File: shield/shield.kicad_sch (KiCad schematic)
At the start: 42 parts, among them J1 Screw_Terminal_01x02, J2 Screw_Terminal_01x02, J3 IC Side 1, J4 IC Side 2, J5 Power Side 1, J6 Power Side 2, Q1 GAN3R2-100CBE, Q2 GAN3R2-100CBE, U1 LM74900

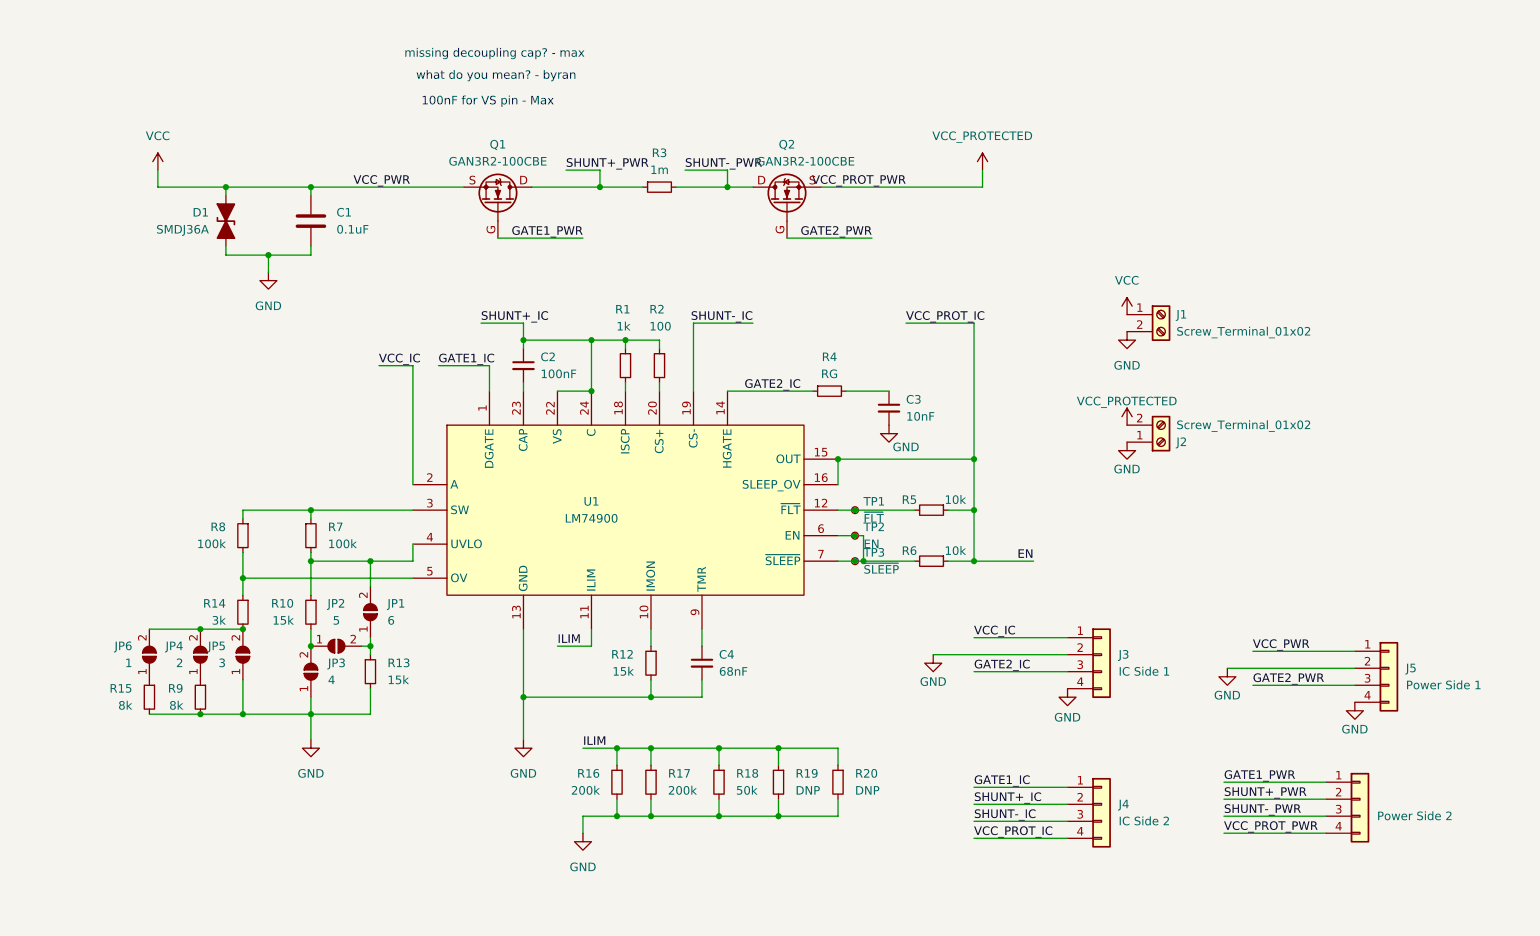
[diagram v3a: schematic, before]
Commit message: Fix: revised shield schematic and pcb
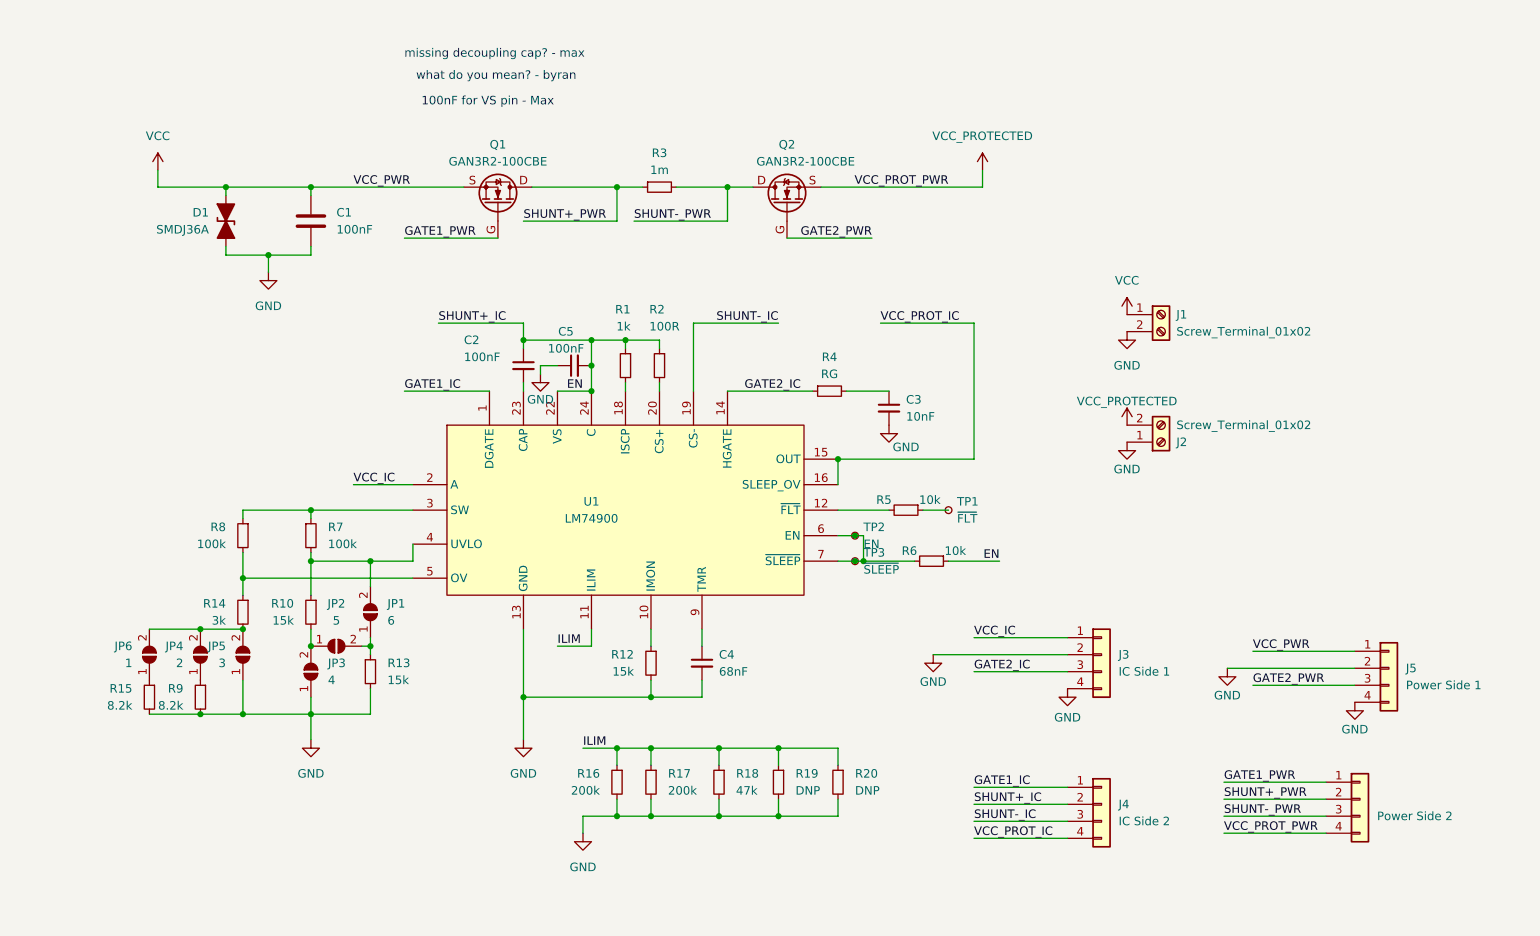
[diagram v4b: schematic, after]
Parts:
- added C5: 100nF, Capacitor_SMD:C_0603_1608Metric, symbol Device:C_Small
- C1: value 0.1uF -> 100nF
- R15, R9: value 8k -> 8.2k
- R18: value 50k -> 47k
- R2: value 100 -> 100R
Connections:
- net SHUNT+_IC is gone; now on net EN: C2.1, J4.2 (Pin_2), R1.1, R2.1, U1.22 (VS), U1.24 (C)
- net EN: now also C5.2; no longer J4.4 (Pin_4), R5.1, U1.15 (OUT), U1.16 (SLEEP_OV)
- net GND: now also C5.1
- net at R5.2, U1.12 (~{FLT}): no longer TP1.1
- new net: R5.1, TP1.1
- new net VCC_PROT_IC: J4.4 (Pin_4), U1.15 (OUT), U1.16 (SLEEP_OV)
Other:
- moved on the sheet: R5, TP1

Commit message: Feat(shield): finished pcb
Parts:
- added Q3, Q4: EPC2304, EPC2304ENGRT:EPC2304_ECC, symbol NFET:Q_NMOS_GSD
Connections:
- net GATE1_PWR: now also Q3.G
- net GATE2_PWR: now also Q4.G
- net SHUNT+_PWR: now also Q3.D
- net SHUNT-_PWR: now also Q4.D
- net VCC: now also Q3.S
- net VCC_PROTECTED: now also Q4.S
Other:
- note removed: "100nF for VS pin - Max"
- note removed: "missing decoupling cap? - max"
- note removed: "what do you mean? - byran"
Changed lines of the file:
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@@
+	(wire
+		(pts
+			(xy 156.21 46.482) (xy 175.26 46.482)
+		)
+		(stroke
+			(width 0)
+			(type default)
+		)
+	)
 	(wire
 		(pts
@@
 	(wire
 		(pts
+			(xy 107.95 54.356) (xy 93.98 54.356)
+		)
+		(stroke
+			(width 0)
+			(type default)
+		)
+	)
+	(wire
+		(pts
 			(xy 93.98 95.25) (xy 106.68 95.25)
 		)
@@
 	(wire
 		(pts
+			(xy 151.13 54.102) (xy 163.83 54.102)
+		)
+		(stroke
+			(width 0)
+			(type default)
+		)
+	)
+	(wire
+		(pts
 			(xy 142.24 95.25) (xy 154.94 95.25)
 		)
@@
 	(wire
 		(pts
+			(xy 132.08 46.482) (xy 146.05 46.482)
+		)
+		(stroke
+			(width 0)
+			(type default)
+		)
+	)
+	(wire
+		(pts
+			(xy 93.218 46.736) (xy 102.87 46.736)
+		)
+		(stroke
+			(width 0)
+			(type default)
+		)
+	)
+	(wire
+		(pts
 			(xy 116.84 91.44) (xy 114.3 91.44)
 		)
@@
 	(wire
 		(pts
+			(xy 127 46.736) (xy 113.03 46.736)
+		)
+		(stroke
+			(width 0)
+			(type default)
+		)
+	)
+	(wire
+		(pts
 			(xy 220.726 134.112) (xy 235.966 134.112)
 		)
@@
 			(width 0)
 			(type default)
-		)
-	)
-	(text "100nF for VS pin - Max"
-		(exclude_from_sim no)
-		(at 106.426 52.07 0)
-		(effects
-			(font
-				(size 1.27 1.27)
-			)
-		)
-	)
-	(text "what do you mean? - byran"
-		(exclude_from_sim no)
-		(at 107.696 48.26 0)
-		(effects
-			(font
-				(size 1.27 1.27)
-			)
-		)
-	)
-	(text "missing decoupling cap? - max"
-		(exclude_from_sim no)
-		(at 107.442 44.958 0)
-		(effects
-			(font
-				(size 1.27 1.27)
-			)
 		)
 	)
@@
 		)
 	)
+	(label "GATE2_PWR"
+		(at 163.83 54.102 180)
+		(fields_autoplaced yes)
+		(effects
+			(font
+				(size 1.27 1.27)
+			)
+			(justify right bottom)
+		)
+	)
+	(label "SHUNT+_PWR"
+		(at 127 46.736 180)
+		(fields_autoplaced yes)
+		(effects
+			(font
+				(size 1.27 1.27)
+			)
+			(justify right bottom)
+		)
+	)
+	(label "SHUNT-_PWR"
+		(at 132.08 46.482 0)
+		(fields_autoplaced yes)
+		(effects
+			(font
+				(size 1.27 1.27)
+			)
+			(justify left bottom)
+		)
+	)
 	(label "EN"
 		(at 182.88 120.65 180)
@@
 		)
 	)
+	(label "GATE1_PWR"
+		(at 93.98 54.356 0)
+		(fields_autoplaced yes)
+		(effects
+			(font
+				(size 1.27 1.27)
+			)
+			(justify left bottom)
+		)
+	)
 	(label "ILIM"
 		(at 120.65 148.59 0)
@@
 		)
 	)
+	(label "VCC_PROT_PWR"
+		(at 175.26 46.482 180)
+		(fields_autoplaced yes)
+		(effects
+			(font
+				(size 1.27 1.27)
+			)
+			(justify right bottom)
+		)
+	)
 	(label "GATE2_PWR"
 		(at 163.83 72.39 180)
@@
 			)
 			(justify right bottom)
+		)
+	)
+	(label "VCC_PWR"
+		(at 93.218 46.736 0)
+		(fields_autoplaced yes)
+		(effects
+			(font
+				(size 1.27 1.27)
+			)
+			(justify left bottom)
 		)
 	)
@@
 	)
 	(symbol
+		(lib_id "NFET:Q_NMOS_GSD")
+		(at 151.13 49.022 90)
+		(unit 1)
+		(exclude_from_sim no)
+		(in_bom yes)
+		(on_board yes)
+		(dnp no)
+		(property "Reference" "Q4"
+			(at 151.13 40.132 90)
+			(effects
+				(font
+					(size 1.27 1.27)
+				)
+			)
+		)
+		(property "Value" "EPC2304"
+			(at 153.924 42.672 90)
+			(effects
+				(font
+					(size 1.27 1.27)
+				)
+				(justify left)
+			)
+		)
+		(property "Footprint" "EPC2304ENGRT:EPC2304_ECC"
+			(at 148.59 43.942 0)
+			(effects
+				(font
+					(size 1.27 1.27)
+				)
+				(hide yes)
+			)
+		)
+		(property "Datasheet" "~"
+			(at 151.13 49.022 0)
+			(effects
+				(font
+					(size 1.27 1.27)
+				)
+				(hide yes)
+			)
+		)
+		(property "Description" "N-MOSFET transistor, gate/source/drain"
+			(at 151.13 49.022 0)
+			(effects
+				(font
+					(size 1.27 1.27)
+				)
+				(hide yes)
+			)
+		)
+		(pin "G"
+		)
+		(pin "D"
+		)
+		(pin "S"
+		)
+		(instances
+			(project "shield"
+				(path "/5b82dc35-3a33-40e8-9adc-c72e6c4a87f2"
+					(reference "Q4")
+					(unit 1)
+				)
+			)
+		)
+	)
+	(symbol
 		(lib_id "Connector_Generic:Conn_01x04")
 		(at 198.12 156.972 0)
@@
 					(unit 1)
 				)
+			)
+		)
+	)
+	(symbol
+		(lib_id "NFET:Q_NMOS_GSD")
+		(at 107.95 49.276 270)
+		(mirror x)
+		(unit 1)
+		(exclude_from_sim no)
+		(in_bom yes)
+		(on_board yes)
+		(dnp no)
+		(property "Reference" "Q3"
+			(at 107.95 40.386 90)
+			(effects
+				(font
+					(size 1.27 1.27)
+				)
+			)
+		)
+		(property "Value" "EPC2304"
+			(at 107.95 42.926 90)
+			(effects
+				(font
+					(size 1.27 1.27)
+				)
+			)
+		)
+		(property "Footprint" "EPC2304ENGRT:EPC2304_ECC"
+			(at 110.49 44.196 0)
+			(effects
+				(font
+					(size 1.27 1.27)
+				)
+				(hide yes)
+			)
+		)
+		(property "Datasheet" "~"
+			(at 107.95 49.276 0)
+			(effects
+				(font
+					(size 1.27 1.27)
+				)
+				(hide yes)
+			)
+		)
+		(property "Description" "N-MOSFET transistor, gate/source/drain"
+			(at 107.95 49.276 0)
+			(effects
+				(font
+					(size 1.27 1.27)
+				)
+				(hide yes)
+			)
+		)
+		(pin "G"
+		)
+		(pin "D"
+		)
+		(pin "S"
+		)
+		(instances
+			(project "shield"
+				(path "/5b82dc35-3a33-40e8-9adc-c72e6c4a87f2"
+					(reference "Q3")
+					(unit 1)
+				)

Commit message: Fix: panelized shield
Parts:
- R14: value 3k -> 4.22k
- R15, R9: value 8.2k -> 15k
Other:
- note added: "OVLO 14.82V: JP #3 OVLO 5.72V: JP #1, JP #2 OVLO 3.72V: JP #2"
- note added: "Selectable OVLO/UVLO, bridge jumpers:"
- note added: "UVLO 8.6V: JP #4, JP #6 UVLO 4.6V: JP #4 UVLO 2.6V: JP #5"
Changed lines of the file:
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@@
 		)
 	)
+	(text "UVLO 8.6V: JP #4, JP #6\nUVLO 4.6V: JP #4\nUVLO 2.6V: JP #5"
+		(exclude_from_sim no)
+		(at 52.07 165.1 0)
+		(effects
+			(font
+				(size 1.27 1.27)
+			)
+			(justify left)
+		)
+	)
+	(text "OVLO 14.82V: JP #3\nOVLO 5.72V: JP #1, JP #2\nOVLO 3.72V: JP #2"
+		(exclude_from_sim no)
+		(at 52.07 171.45 0)
+		(effects
+			(font
+				(size 1.27 1.27)
+			)
+			(justify left)
+		)
+	)
+	(text "Selectable OVLO/UVLO, bridge jumpers:"
+		(exclude_from_sim no)
+		(at 68.58 160.02 0)
+		(effects
+			(font
+				(size 1.27 1.27)
+				(thickness 0.254)
+				(bold yes)
+				(italic yes)
+			)
+		)
+	)
 	(label "SHUNT-_IC"
 		(at 179.07 159.512 0)
@@
 			)
 		)
-		(property "Value" "8.2k"
+		(property "Value" "15k"
 			(at 60.96 142.2399 0)
 			(effects
@@
 			)
 		)
-		(property "Value" "8.2k"
+		(property "Value" "15k"
 			(at 53.34 142.2399 0)
 			(effects
@@
 			)
 		)
-		(property "Value" "3k"
+		(property "Value" "4.22k"
 			(at 67.31 129.5399 0)
 			(effects

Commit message: Feat[shield]: schematic draft
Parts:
- removed C2, C5: 100nF, Capacitor_SMD:C_0603_1608Metric, symbol Device:C_Small
- removed C3: 10nF, Capacitor_SMD:C_0603_1608Metric, symbol Device:C_Small
- removed C4: 68nF, Capacitor_SMD:C_0603_1608Metric, symbol Device:C_Small
- removed JP4: 2, Jumper:SolderJumper-2_P1.3mm_Open_Pad1.0x1.5mm, symbol Jumper:SolderJumper_2_Open
- removed JP5: 3, Jumper:SolderJumper-2_P1.3mm_Open_Pad1.0x1.5mm, symbol Jumper:SolderJumper_2_Open
- removed JP6: 1, Jumper:SolderJumper-2_P1.3mm_Open_Pad1.0x1.5mm, symbol Jumper:SolderJumper_2_Open
- removed R10, R12, R13, R15: 15k, Resistor_SMD:R_0402_1005Metric, symbol Device:R_Small
- removed R14: 4.22k, Resistor_SMD:R_0402_1005Metric, symbol Device:R_Small
- removed R16, R17: 200k, Resistor_SMD:R_0402_1005Metric, symbol Device:R_Small
- removed R18: 47k, Resistor_SMD:R_0402_1005Metric, symbol Device:R_Small
- removed R19, R20: DNP, Resistor_SMD:R_0603_1608Metric, symbol Device:R_Small
- removed TP1: ~{FLT}, TestPoint:TestPoint_Pad_1.0x1.0mm, symbol Connector:TestPoint_Small
- removed TP2: EN, TestPoint:TestPoint_Pad_1.0x1.0mm, symbol Connector:TestPoint_Small
- removed TP3: ~{SLEEP}, TestPoint:TestPoint_Pad_1.0x1.0mm, symbol Connector:TestPoint_Small
- removed U1: LM74900, Package_DFN_QFN:VQFN-24-1EP_4x4mm_P0.5mm_EP2.5x2.5mm, symbol LM74900:LM74900
- added C2, C4: 100nF, Capacitor_SMD:C_1206_3216Metric, symbol Device:C
- added C3: 10nF, Capacitor_SMD:C_1206_3216Metric, symbol Device:C
- added C5: 47uF, Capacitor_SMD:C_1206_3216Metric, symbol Device:C
- added U1: LM74810QDRRRQ1, SON50P300X300X80-13N-D, symbol LM74810QDRRRQ1:LM74810QDRRRQ1
- JP1: value 6 -> SolderJumper_2_Open; footprint Jumper:SolderJumper-2_P1.3mm_Open_Pad1.0x1.5mm -> (none)
- JP2: value 5 -> SolderJumper_2_Open; footprint Jumper:SolderJumper-2_P1.3mm_Open_Pad1.0x1.5mm -> (none)
- JP3: value 4 -> SolderJumper_2_Open; footprint Jumper:SolderJumper-2_P1.3mm_Open_Pad1.0x1.5mm -> (none)
- Q1, Q2: value GAN3R2-100CBE -> IRFB3077PbF
- Q3, Q4: value EPC2304 -> IPB020N10N5LF; footprint EPC2304ENGRT:EPC2304_ECC -> WLCSP8-SOT8072:WLCSP8-SOT8072
- R1: value 1k -> 22kΩ; footprint Resistor_SMD:R_0402_1005Metric -> (none)
- R2: value 100R -> 22kΩ; footprint Resistor_SMD:R_0402_1005Metric -> (none)
- R3: value 1m -> 3.3kΩ; footprint Resistor_SMD:R_2512_6332Metric -> (none)
- R4: value RG -> 100kΩ; footprint Resistor_SMD:R_0402_1005Metric -> (none)
- R5: value 10k -> 220kΩ; footprint Resistor_SMD:R_0402_1005Metric -> (none)
- R6: value 10k -> 82kΩ; footprint Resistor_SMD:R_0402_1005Metric -> (none)
- R7: value 100k -> 18kΩ; footprint Resistor_SMD:R_0402_1005Metric -> (none)
- R8: value 100k -> 3.3kΩ; footprint Resistor_SMD:R_0402_1005Metric -> (none)
- R9: value 15k -> 82kΩ; footprint Resistor_SMD:R_0402_1005Metric -> (none)
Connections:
- net SHUNT-_IC is gone; now on net VCC_PROT_IC: J4.3 (Pin_3)
- net GND: now also JP3.2 (B), R3.2, R8.2, C3.2, C4.2, C5.2, U1.7 (GND); no longer JP3.1 (A), R9.2
- net VCC: now also U1.2 (A), U1.3 (VSNS); no longer J5.1 (Pin_1), Q3.S
- net VCC_PROTECTED: now also J6.3 (Pin_3), C5.1; no longer Q4.S
- net at R6.2: now also JP2.1 (A)
- net EN/UVLO: now reaches R8.1
- net EN/UVLO: now also R7.2, U1.6 (EN/UVLO); no longer R7.1
- net OV: now reaches JP1.2 (B)
- net OV: now also JP2.2 (B), R2.2, R3.1, U1.5 (OV); no longer R7.2
- net at JP1.1 (A): now also R5.2; no longer JP2.2 (B)
- net SW: now reaches R5.1
- net SW: now also R1.1, R6.1, R7.1, R9.1, U1.4 (SW)
- net HGATE: now reaches R4.2
- net HGATE: now also Q2.G, Q4.G, U1.8 (HGATE)
- net at R1.2: now also R2.1
- removed net EN: J4.2 (Pin_2), R1.1, R2.1, R6.1
- net GATE1_IC renamed DGATE_IC
- net DGATE_IC: now also J4.2 (Pin_2)
- net GATE1_PWR renamed DGATE
- net DGATE: now also U1.1 (DGATE); no longer J6.1 (Pin_1)
- net GATE2_IC: no longer names the net of R4.1
- net GATE2_IC: now also C3.1; no longer J3.3 (Pin_3)
- removed net GATE2_PWR: J5.3 (Pin_3), Q2.G, Q4.G
- removed net SHUNT+_PWR: J6.2 (Pin_2), Q1.D, Q3.D, R3.1
- removed net SHUNT-_PWR: J6.3 (Pin_3), Q2.D, Q4.D, R3.2
- new net: JP3.1 (A), R9.2
- new net C: C2.1, C4.1, Q1.D, Q2.D, U1.10 (VS), U1.12 (C)
- new net CAP: C2.2, U1.11 (CAP)
- new net DGATE_PWR: J5.3 (Pin_3)
- new net HGATE_IC: J3.3 (Pin_3)
- new net HGATE_PWR: J6.1 (Pin_1), J6.2 (Pin_2)
- new net OUT: U1.9 (OUT)
- new net VCC_PWR: J5.1 (Pin_1)
- no-connect marks 0 -> 1
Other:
- note added: "DEFAULT OVLO 17.77V +JP1 14.77V +JP2 12.00V +JP1 +JP2 10.76V"
- note added: "DEFAULT UVLO 8.00V +JP3 6.70V"
- note added: "Infineon Linear FETs"
- note removed: "OVLO 14.82V: JP #3 OVLO 5.72V: JP #1, JP #2 OVLO 3.72V: JP #2"
- note removed: "Selectable OVLO/UVLO, bridge jumpers:"
- note removed: "UVLO 8.6V: JP #4, JP #6 UVLO 4.6V: JP #4 UVLO 2.6V: JP #5"
- moved on the sheet: C1, D1, J1, J2, J3, J4, J5, Q1, Q2

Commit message: Feat[shield]: add leds
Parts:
- added D2, D3: LED, symbol Device:LED
- added R10, R11: 3.3kΩ, symbol Device:R_Small
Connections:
- net C: now also R11.1
- net GND: now also D2.1 (K), D3.1 (K)
- net VCC_PROTECTED: now also R10.1
- new net: D3.2 (A), R11.2
- new net: D2.2 (A), R10.2
